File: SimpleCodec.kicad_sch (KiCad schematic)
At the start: 3 parts

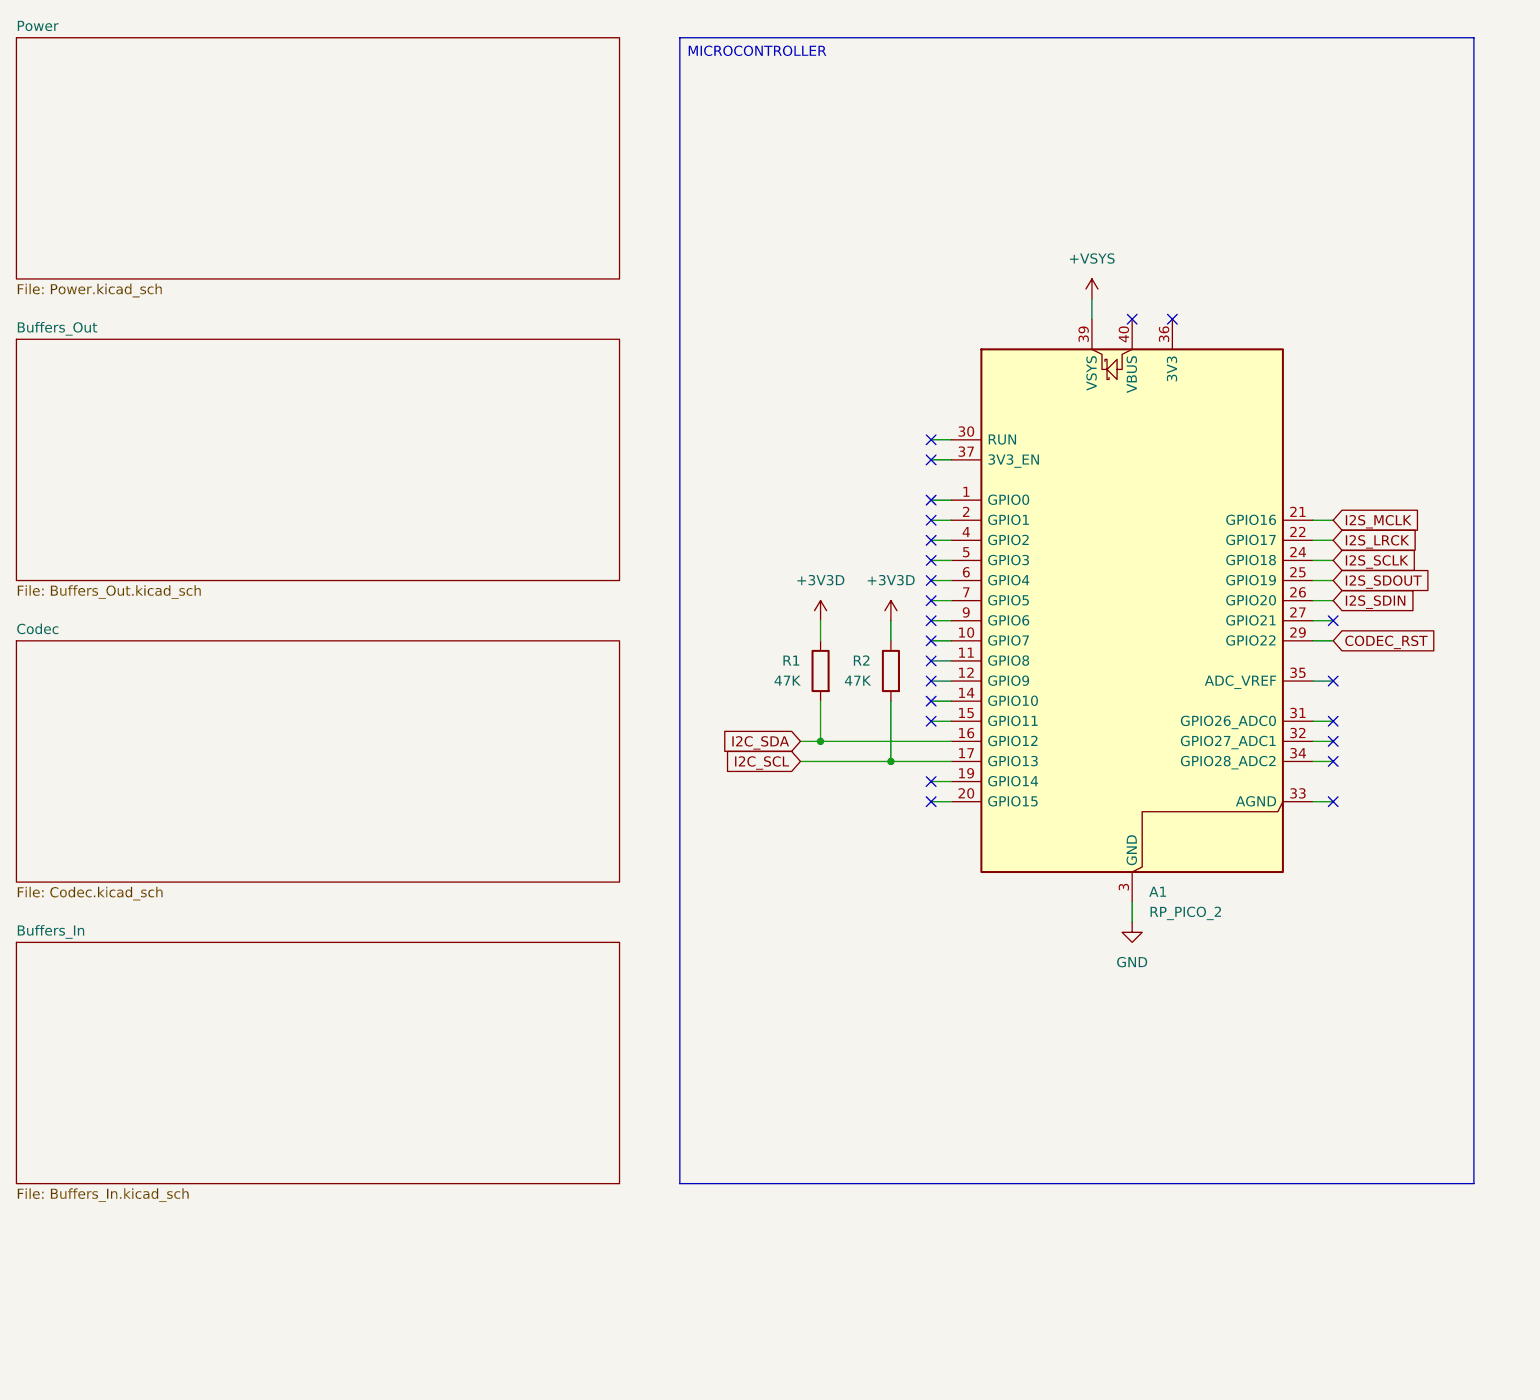
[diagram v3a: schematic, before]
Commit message: Initial layout
Initial layout inside a 1590N1/125B pedal enclosure.
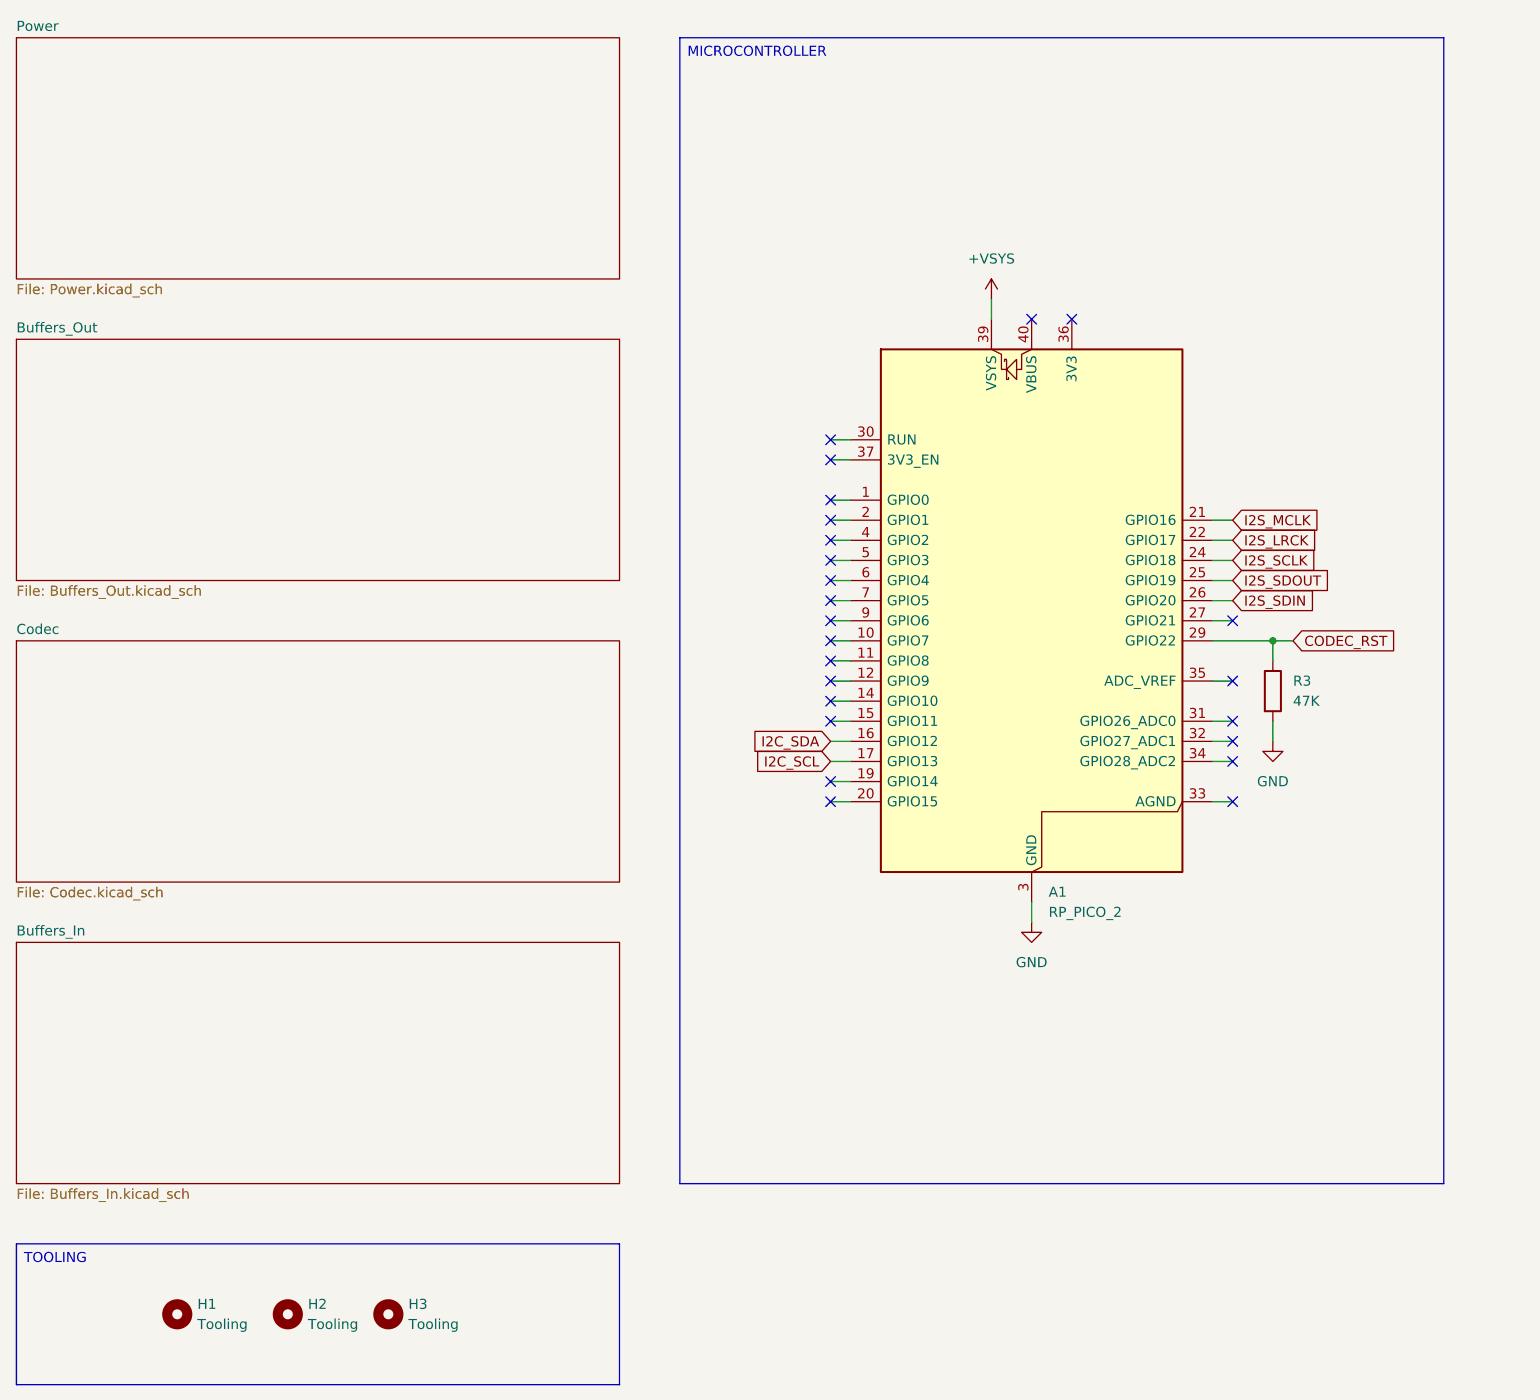
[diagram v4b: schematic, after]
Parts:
- removed R1, R2: 47K, Resistor_SMD:R_0603_1608Metric, symbol Device:R
- added H1, H2, H3: Tooling, MountingHole:ToolingHole_1.152mm, symbol Mechanical:MountingHole
- added R3: 47K, Resistor_SMD:R_0603_1608Metric, symbol Device:R
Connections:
- net CODEC_RST: now also R3.1
- net GND: now also R3.2
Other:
- moved on the sheet: A1

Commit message: RP2350 layout
Updated the layout for the RP2350.
Added board headers.
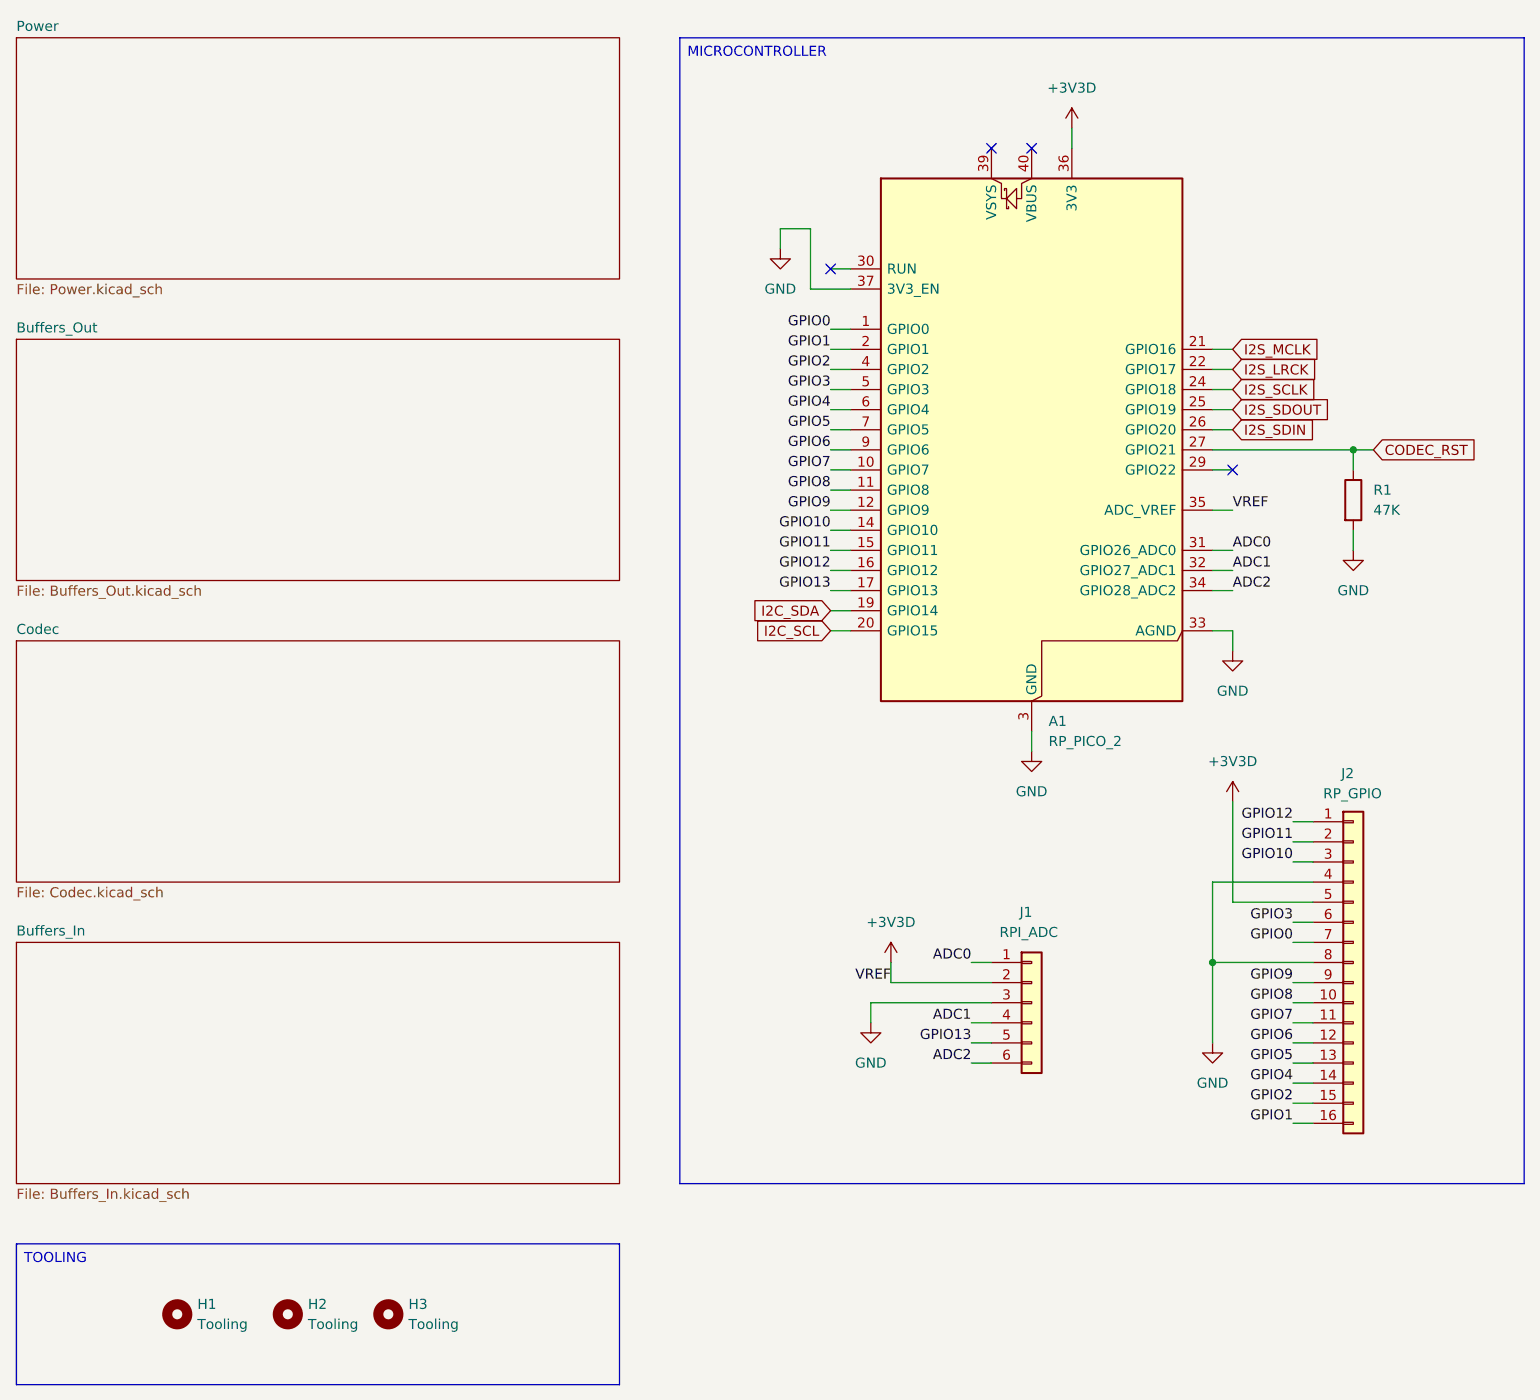
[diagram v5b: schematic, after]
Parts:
- added J1: RPI_ADC, Custom_Parts:HEADER_THROUGH_2x03_P2.54mm, symbol Connector_Generic:Conn_01x06
- added J2: RP_GPIO, Custom_Parts:HEADER_THROUGH_2x08_P2.54mm, symbol Connector_Generic:Conn_01x16
- renumbered R3 to R1
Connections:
- net CODEC_RST: now also A1.27 (GPIO21); no longer A1.29 (GPIO22)
- net GND: now also A1.33 (AGND), A1.37 (3V3_EN), J1.3 (Pin_3), J2.4 (Pin_4), J2.8 (Pin_8)
- net I2C_SCL: now also A1.20 (GPIO15); no longer A1.17 (GPIO13)
- net I2C_SDA: now also A1.19 (GPIO14); no longer A1.16 (GPIO12)
- net GPIO0: now reaches A1.1 (GPIO0)
- net GPIO0: now also J2.7 (Pin_7)
- net GPIO7: now reaches A1.10 (GPIO7)
- net GPIO7: now also J2.11 (Pin_11)
- net GPIO8: now reaches A1.11 (GPIO8)
- net GPIO8: now also J2.10 (Pin_10)
- net GPIO9: now reaches A1.12 (GPIO9)
- net GPIO9: now also J2.9 (Pin_9)
- net GPIO10: now reaches A1.14 (GPIO10)
- net GPIO10: now also J2.3 (Pin_3)
- net GPIO11: now reaches A1.15 (GPIO11)
- net GPIO11: now also J2.2 (Pin_2)
- net GPIO1: now reaches A1.2 (GPIO1)
- net GPIO1: now also J2.16 (Pin_16)
- net ADC0: now reaches A1.31 (GPIO26_ADC0)
- net ADC0: now also J1.1 (Pin_1)
- net ADC1: now reaches A1.32 (GPIO27_ADC1)
- net ADC1: now also J1.4 (Pin_4)
- net ADC2: now reaches A1.34 (GPIO28_ADC2)
- net ADC2: now also J1.6 (Pin_6)
- net +3V3D: now reaches A1.35 (ADC_VREF)
- net +3V3D: now also A1.36 (3V3), J1.2 (Pin_2), J2.5 (Pin_5)
- net GPIO2: now reaches A1.4 (GPIO2)
- net GPIO2: now also J2.15 (Pin_15)
- net GPIO3: now reaches A1.5 (GPIO3)
- net GPIO3: now also J2.6 (Pin_6)
- net GPIO4: now reaches A1.6 (GPIO4)
- net GPIO4: now also J2.14 (Pin_14)
- net GPIO5: now reaches A1.7 (GPIO5)
- net GPIO5: now also J2.13 (Pin_13)
- net GPIO6: now reaches A1.9 (GPIO6)
- net GPIO6: now also J2.12 (Pin_12)
- net +VSYS: no longer names the net of A1.39 (VSYS)
- new net GPIO12: A1.16 (GPIO12), J2.1 (Pin_1)
- new net GPIO13: A1.17 (GPIO13), J1.5 (Pin_5)
- no-connect marks 24 -> 4
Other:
- moved on the sheet: A1, R1
